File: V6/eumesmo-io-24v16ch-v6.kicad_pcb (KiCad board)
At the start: 4 copper layers, 128 x 67.8 mm, 341 parts, among them J1 250-208, J2 250-208, J3 250-208, J4 250-208, J5 250-202, J6 250-202, J7 USB_C_Receptacle_USB2.0, J8 ETHERNET, J9 250-203, Q1 WPM2015-3/TR, Q10 MMBT2222A, Q11 MMBT2222A, Q12 MMBT2222A, Q13 MMBT2222A, Q14 MMBT2222A, Q15 MMBT2222A, Q16 MMBT2222A, Q17 MMBT2222A, Q18 MMBT2222A, Q19 MMBT2222A, Q2 MMUN2211LT3G, Q3 UMH3N, Q4 MMBT2222A, Q5 MMBT2222A, Q6 MMBT2222A, Q7 MMBT2222A, Q8 MMBT2222A, Q9 MMBT2222A, SW1 RESET, SW2 1WIRE_SEL, U1 TX4138, U10 MCP23017, U11 DS2482S-100, U12 OR-3H7-4, U13 OR-3H7-4, U14 OR-3H7-4, U15 OR-3H7-4, U2 SY8089A1AAC, U3 TPS3820-33, U4 CH340K, U5 ESP32-WROOM-32UE-N16, U6 LAN8710A, U7 TPS3823-33, U8 MCP23008, U9 MCP23008

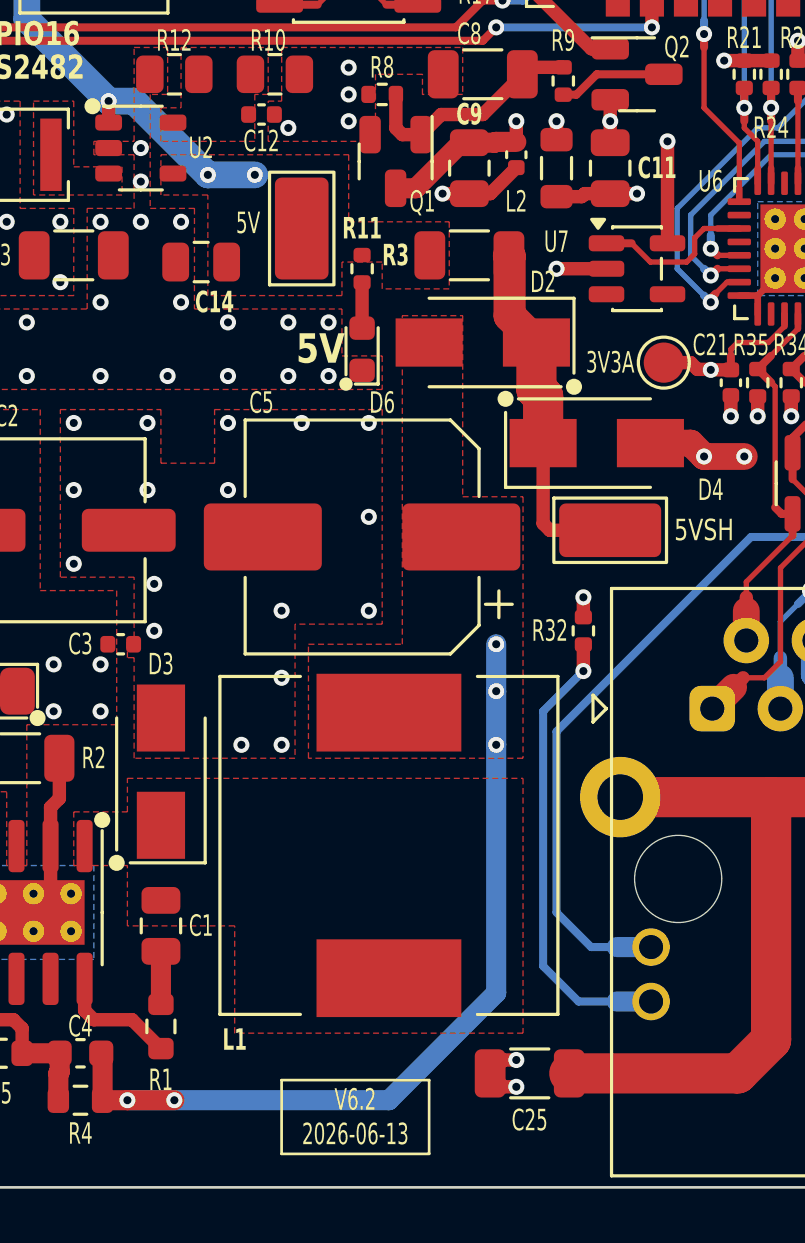
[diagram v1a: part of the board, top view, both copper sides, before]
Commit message: Widened tracks at pads and vias.
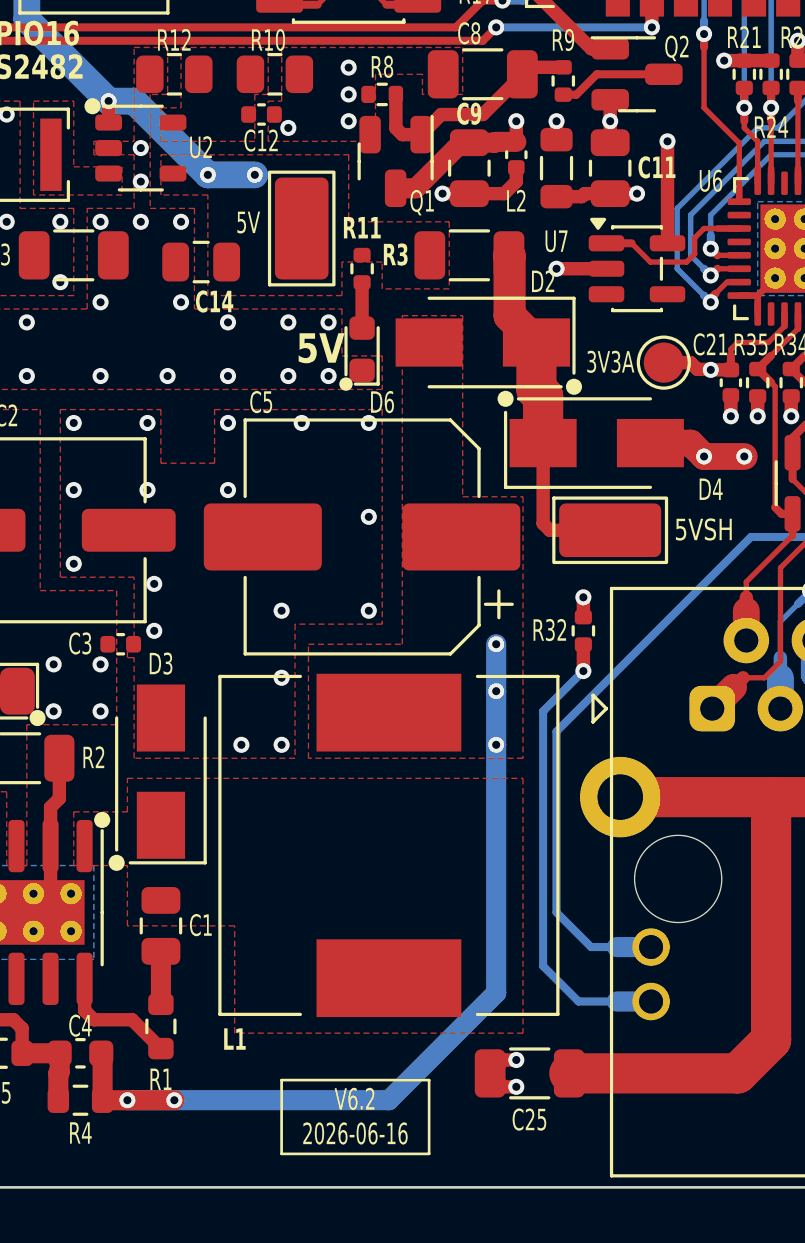
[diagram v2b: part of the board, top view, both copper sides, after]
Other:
- board text added: "V6.2 2026-06-16"
- board text removed: "V6.2 2026-06-13"
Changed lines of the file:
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@@
 		(layer "Edge.Cuts")
 	)
-	(gr_text "V6.2\n2026-06-13"
+	(gr_text "V6.2\n2026-06-16"
 		(at 158.52 131.455 0)
 		(layer "F.SilkS")
@@
 	)
 	(segment
-		(start 163.55 97.03)
-		(end 164.52 96.06)
-		(width 0.5)
-		(layer "F.Cu")
-		(net "GND")
-	)
-	(segment
 		(start 206.07 117.58)
 		(end 206.07 116.33)
@@
 	)
 	(segment
-		(start 162.77 97.03)
-		(end 163.55 97.03)
-		(width 0.5)
-		(layer "F.Cu")
-		(net "GND")
-	)
-	(segment
 		(start 190.27 76.58)
 		(end 189.53 76.58)
@@
 	)
 	(segment
+		(start 162.77 97.03)
+		(end 164.07 97.03)
+		(width 0.5)
+		(layer "F.Cu")
+		(net "GND")
+	)
+	(segment
 		(start 201.77 74.08)
 		(end 200.97 74.08)
@@
 	)
 	(segment
+		(start 164.52 96.58)
+		(end 164.52 96.06)
+		(width 0.5)
+		(layer "F.Cu")
+		(net "GND")
+	)
+	(segment
 		(start 211.27 110.58)
 		(end 210.53 110.58)
@@
 		(width 0.5)
 		(layer "F.Cu")
+		(net "GND")
+	)
+	(segment
+		(start 164.07 97.03)
+		(end 164.52 96.58)
+		(width 0.5)
+		(layer "F.Cu")

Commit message: Release V6.2.0
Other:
- board text added: "V6.2 2026-06-17"
- board text removed: "V6.2 2026-06-16"
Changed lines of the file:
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@@
 	(title_block
 		(title "eumesmo 24V 16xIn/16xOut/1-Wire Module")
-		(date "2026-06-13")
+		(date "2026-06-17")
 		(rev "V6.2")
 	)
@@
 	)
 	(gr_rect
-		(start 155.77 130.08)
-		(end 161.27 132.83)
+		(start 156.02 132.455)
+		(end 163.52 133.705)
 		(stroke
 			(width 0.1)
@@
 		(layer "Edge.Cuts")
 	)
-	(gr_text "V6.2\n2026-06-16"
-		(at 158.52 131.455 0)
+	(gr_text "V6.2 2026-06-17"
+		(at 159.77 133.08 0)
 		(layer "F.SilkS")
 		(effects
